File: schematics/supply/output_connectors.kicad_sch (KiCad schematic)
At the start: 38 parts, among them J14 Conn_01x05_Pin, J15 banana jack + fuse 15A, J16 banana jack + fuse 15A, J17 Conn_01x05_Pin, J18 Conn_01x02_Pin, J19 Conn_01x02_Pin, J20 Conn_02x04_Odd_Even, J21 jst xh angle, J22 jst xh angle, Q10 IRLML0030, Q10 IRLML5203, U20 TP4056, U6 INA3221

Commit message: Found and fixed issues in schematics.
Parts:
- R54: value 2K -> 510
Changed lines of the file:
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@@
       (effects (font (size 1.27 1.27)) (justify left))
     )
-    (property "Value" "2K" (at 166.37 201.93 0)
+    (property "Value" "510" (at 166.37 201.93 0)
       (effects (font (size 1.27 1.27)) (justify left))
     )

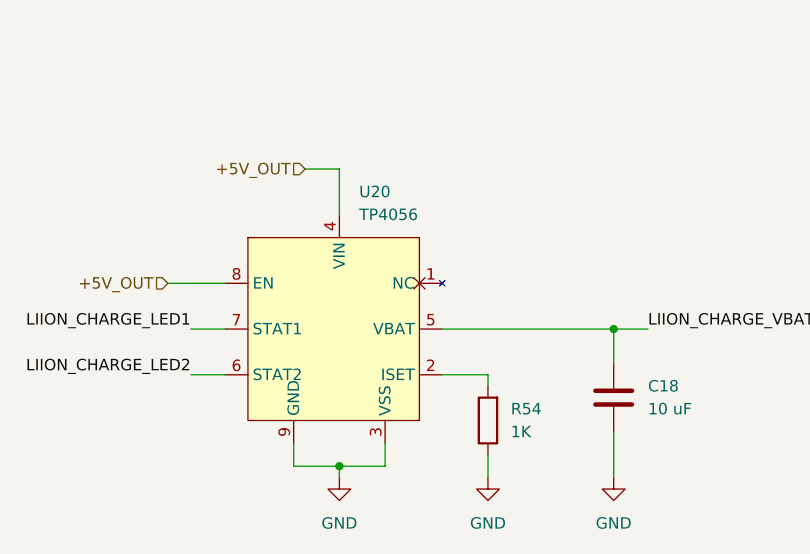
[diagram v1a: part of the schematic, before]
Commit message: fix pins in firmware
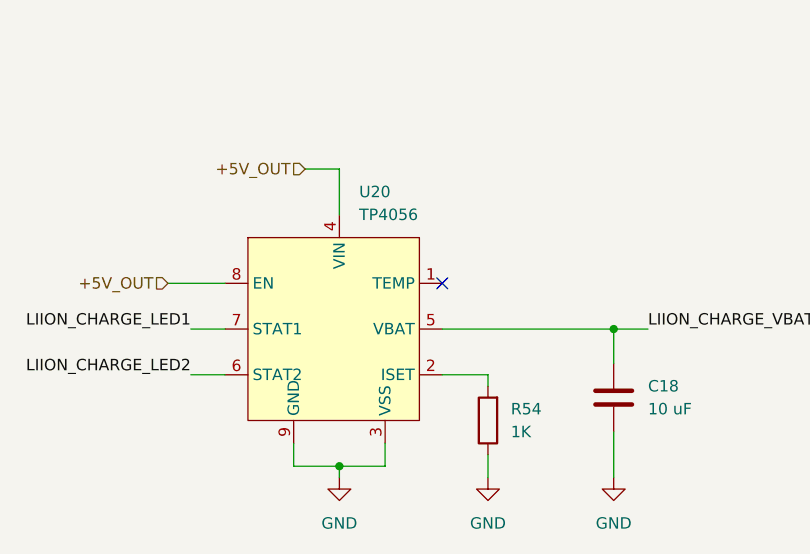
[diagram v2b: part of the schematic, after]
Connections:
- no-connect marks 8 -> 9
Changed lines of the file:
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@@
   (no_connect (at 203.2 52.07))
   (no_connect (at 186.69 119.38))
+  (no_connect (at 92.71 209.55))
   (no_connect (at 210.82 52.07))
   (no_connect (at 201.93 29.21))

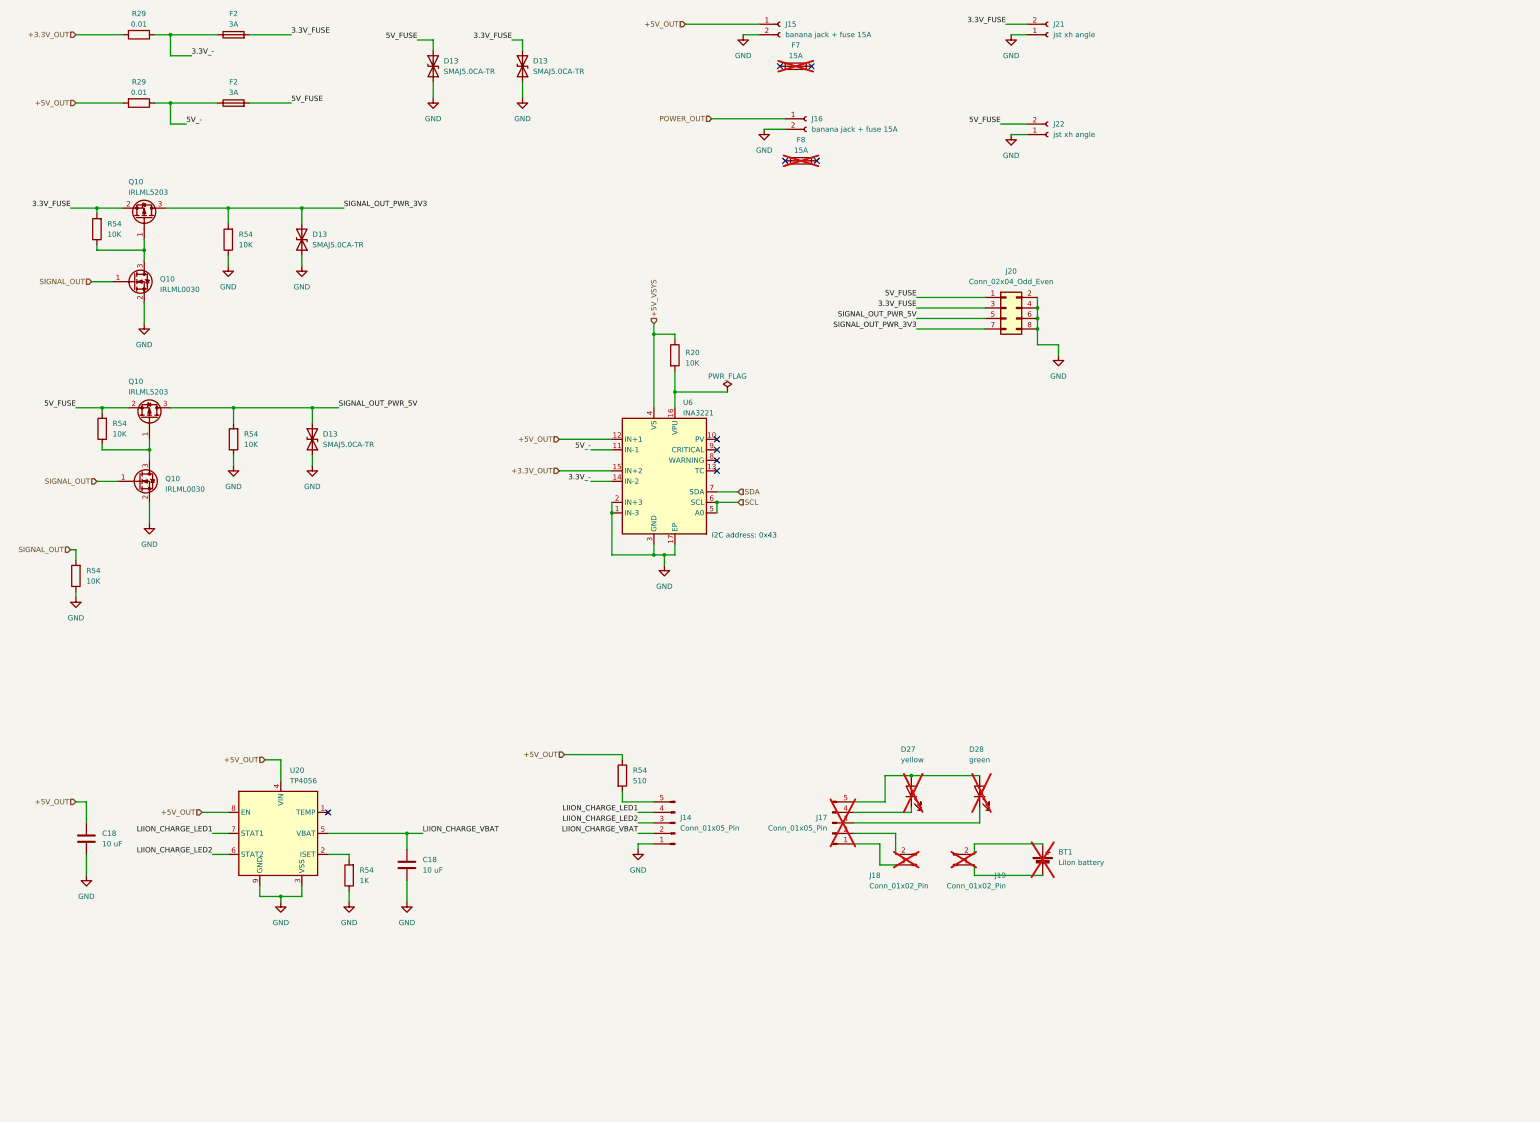
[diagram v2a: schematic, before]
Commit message: supply board - power controllers changed; PWM logic changed
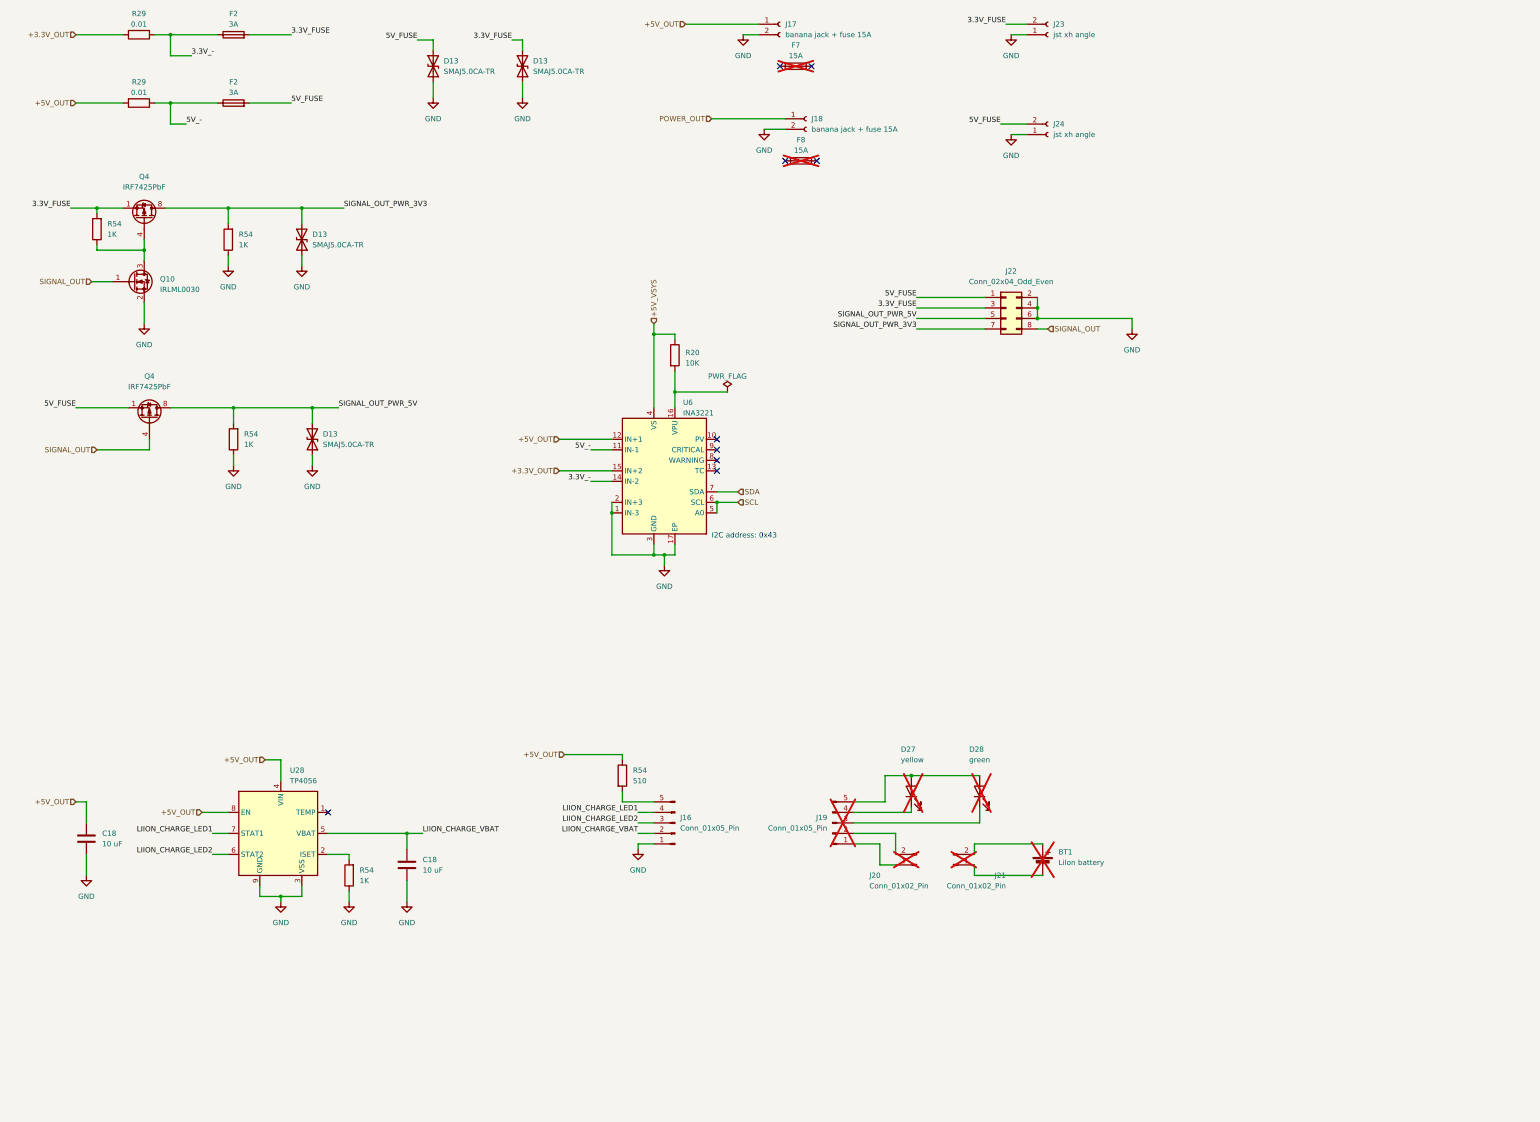
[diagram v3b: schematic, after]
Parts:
- removed Q10: IRLML0030, Package_TO_SOT_SMD:SOT-23, symbol Transistor_FET:IRLML0030
- removed Q10 (x2): IRLML5203, Package_TO_SOT_SMD:SOT-23, symbol Transistor_FET:IRLML5203
- removed R54 (x2): 10K, Resistor_SMD:R_0805_2012Metric, symbol Device:R
- added Q4 (x2): IRF7425PbF, Package_SO:SOIC-8_3.9x4.9mm_P1.27mm, symbol Transistor_FET:IRF7404
- R54: value 10K -> 1K
- renumbered J14 to J16, J15 to J17, J16 to J18, J17 to J19, J18 to J20, J19 to J21, J20 to J22, J21 to J23, J22 to J24, U20 to U28
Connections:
- net 3.3V_FUSE: now also Q4.1 (S), Q4.2 (S), Q4.3 (S)
- net 5V_FUSE: now also Q4.1 (S), Q4.2 (S), Q4.3 (S)
- net GND: no longer J22.8 (Pin_8)
- net SIGNAL_OUT: now also J22.8 (Pin_8), Q4.4 (G)
- net SIGNAL_OUT_PWR_3V3: now also Q4.5 (D), Q4.6 (D), Q4.7 (D), Q4.8 (D)
- net SIGNAL_OUT_PWR_5V: now also Q4.5 (D), Q4.6 (D), Q4.7 (D), Q4.8 (D)
- net at Q10.3 (D), R54.1: now also Q4.4 (G)

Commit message: re-design supply board
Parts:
- renumbered J16 to J20, J17 to J21, J18 to J22, J19 to J23, J20 to J24, J21 to J25, J22 to J26, J23 to J27, J24 to J28

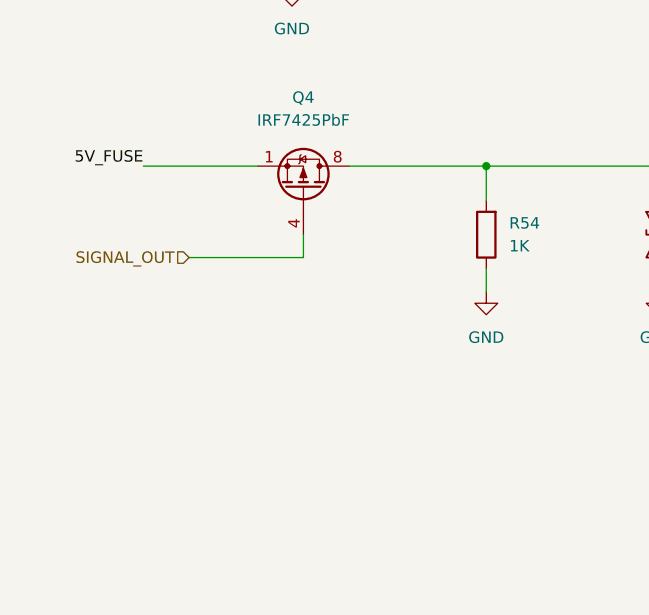
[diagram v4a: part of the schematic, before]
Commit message: Fixed error on board, v1.3 ordered
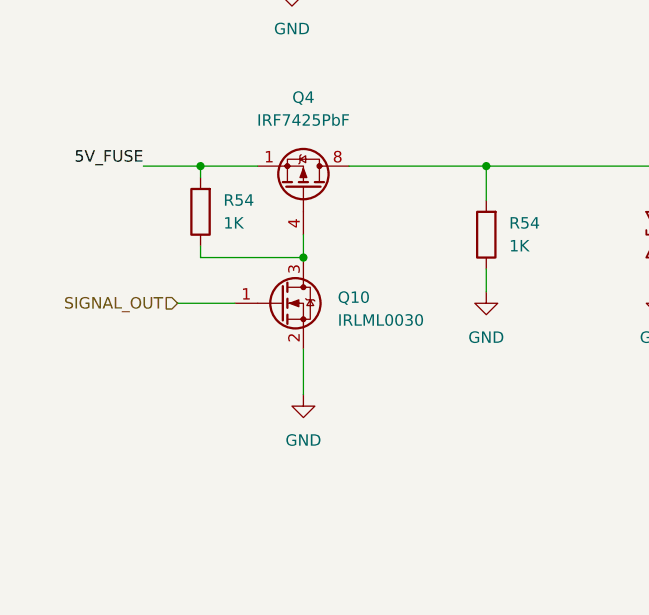
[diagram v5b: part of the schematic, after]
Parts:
- added Q10: IRLML0030, Package_TO_SOT_SMD:SOT-23, symbol Transistor_FET:IRLML0030
- added R54: 1K, Resistor_SMD:R_0805_2012Metric, symbol Device:R
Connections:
- net 5V_FUSE: now also R54.2
- net GND: now also Q10.2 (S)
- net SIGNAL_OUT: now also Q10.1 (G); no longer Q4.4 (G)
- new net: Q10.3 (D), Q4.4 (G), R54.1

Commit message: Continue project
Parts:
- U29: renamed from U6; footprint Package_DFN_QFN:Texas_RGV_S-PVQFN-N16_EP2.1x2.1mm -> Package_DFN_QFN:Texas_RGV0016A_VQFN-16-1EP_4x4mm_P0.65mm_EP2.1x2.1mm
- renumbered C18 to C64, C18 to C65, D13 to D23, D13 to D24, D13 to D25, D13 to D26, F2 to F5, F2 to F6, Q10 to Q12, Q10 to Q15, R54 to R63, R29 to R64, R29 to R65, R54 to R66, R54 to R67, R54 to R68, R54 to R69, R20 to R70, R54 to R71

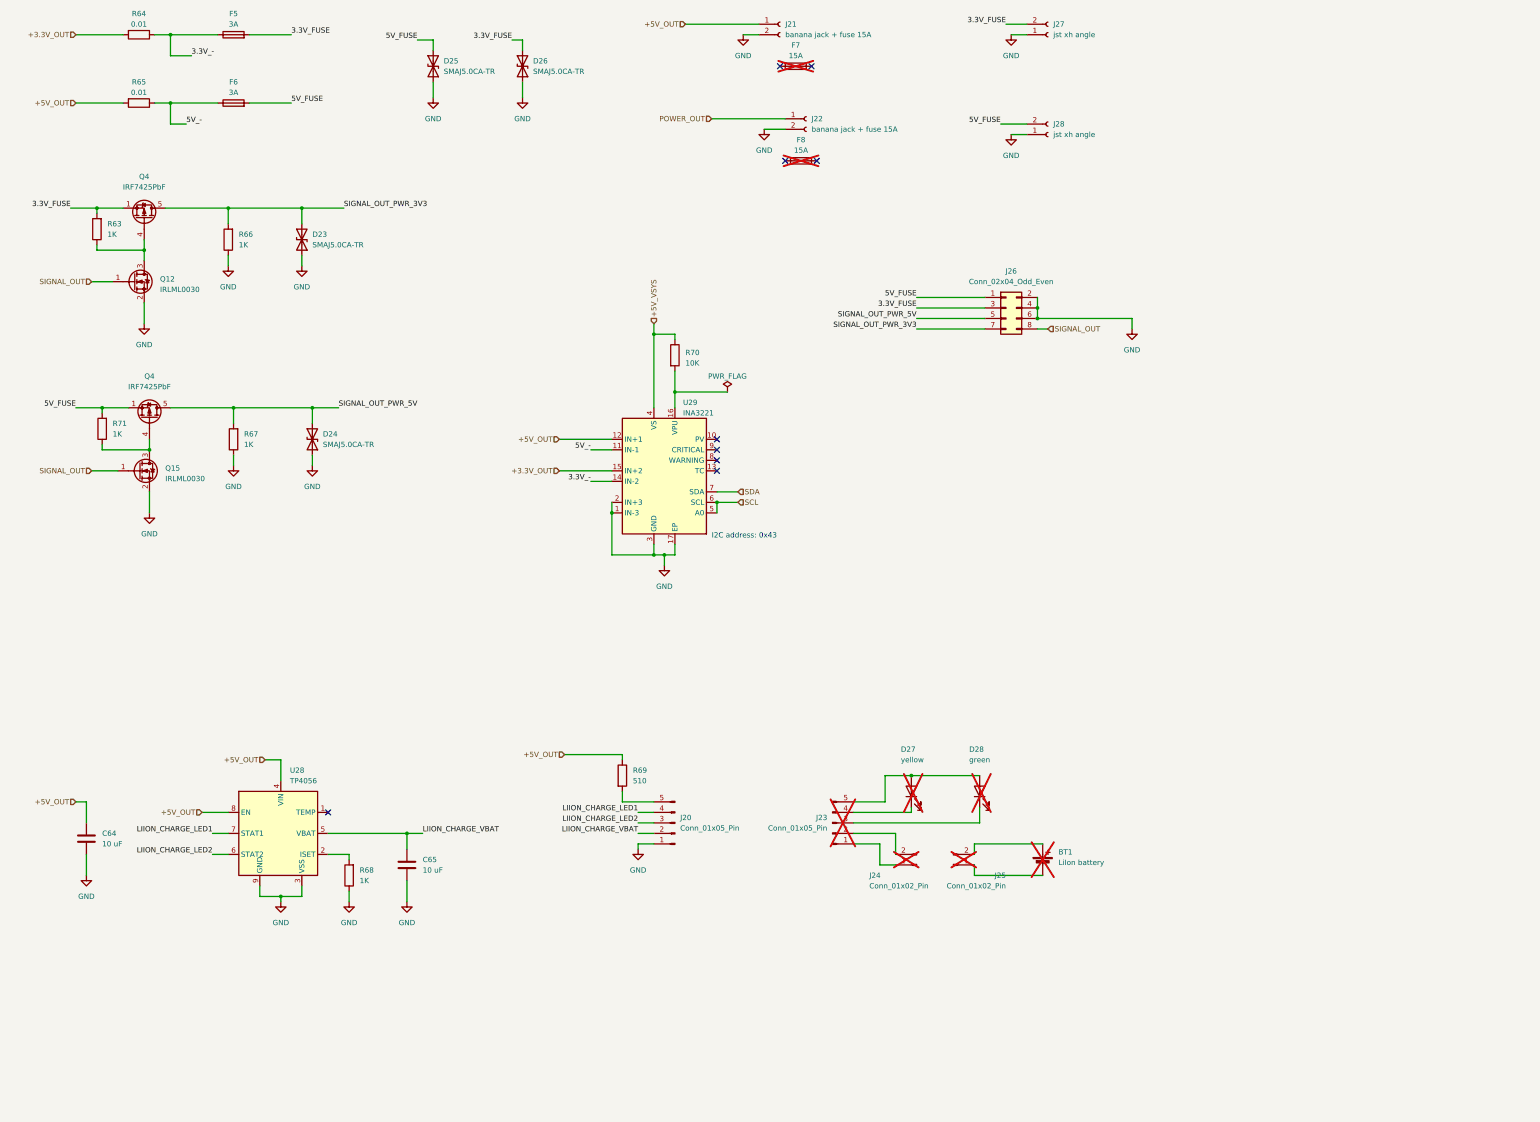
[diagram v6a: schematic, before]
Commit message: debugging DCDC converters... Standby supply works fine (noise level = 1,7%). At now Starting to debug PFC module
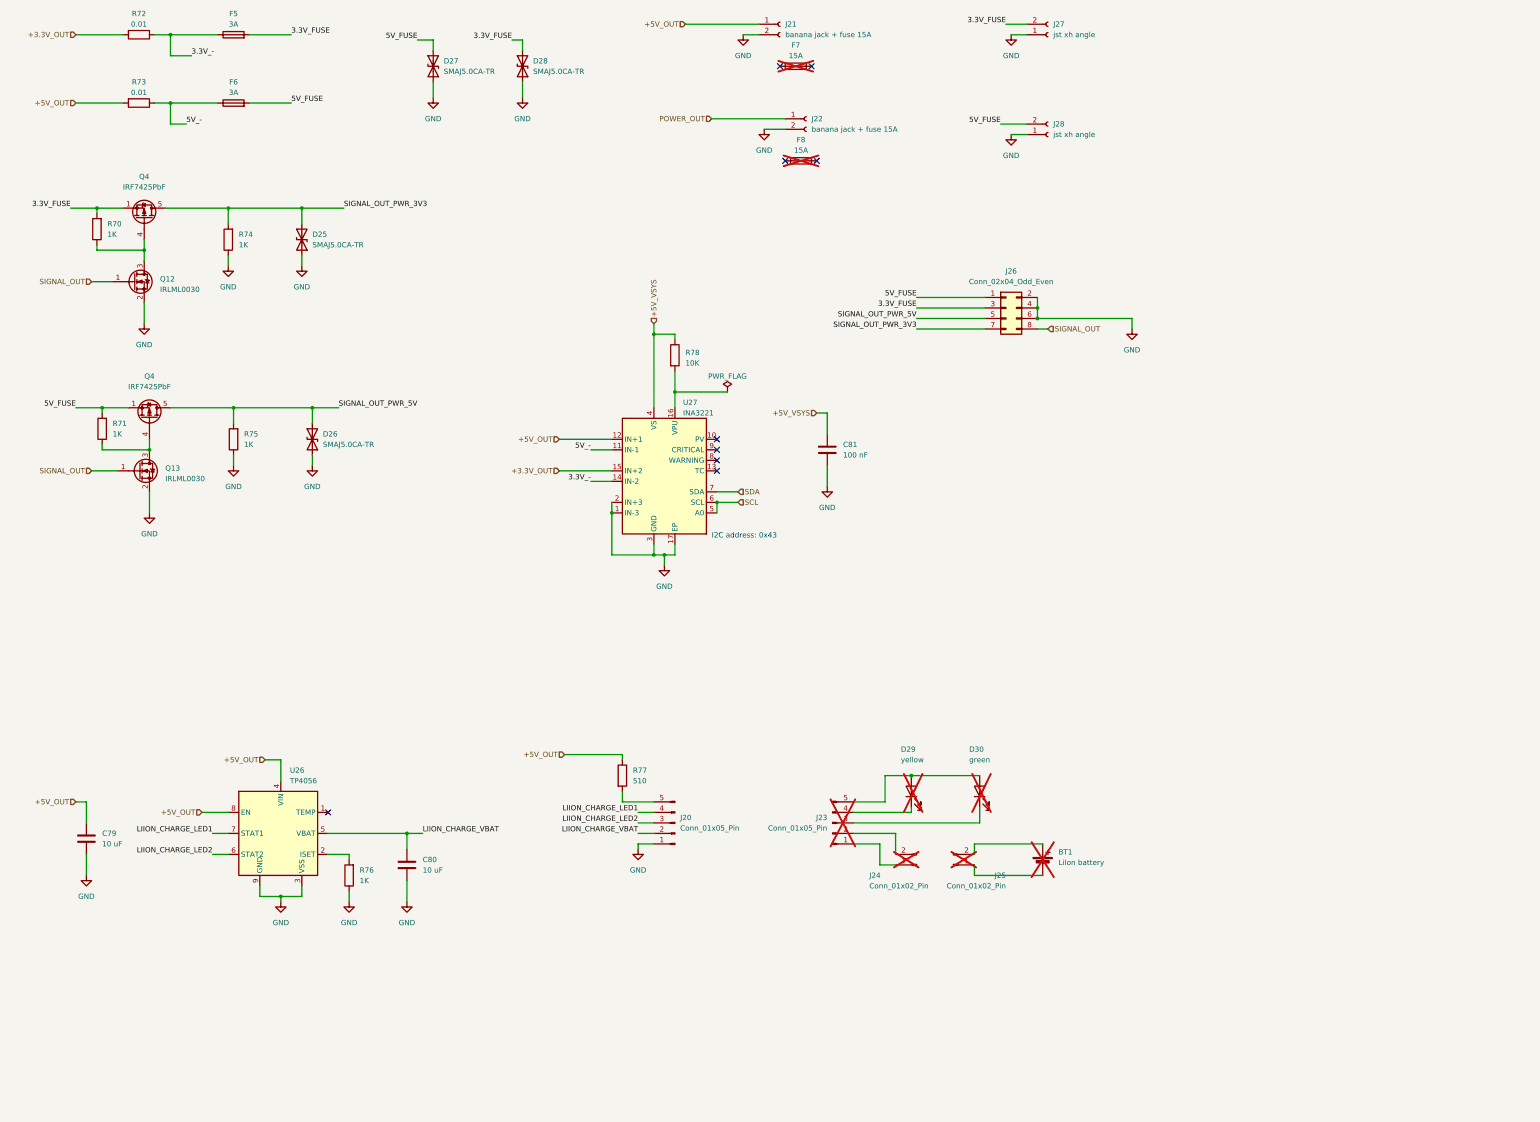
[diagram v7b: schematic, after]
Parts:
- added C81: 100 nF, Capacitor_SMD:C_0603_1608Metric, symbol Device:C
- renumbered C64 to C79, C65 to C80, D23 to D25, D24 to D26, D25 to D27, D26 to D28, D27 to D29, D28 to D30, Q15 to Q13, R63 to R70, R64 to R72, R65 to R73, R66 to R74, R67 to R75, R68 to R76, R69 to R77, R70 to R78, U28 to U26, U29 to U27
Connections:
- net +5V_VSYS: now also C81.2
- net GND: now also C81.1
